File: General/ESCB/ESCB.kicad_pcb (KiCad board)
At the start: 2 copper layers, 37.4 x 21.6 mm, 3 parts, among them J1 Power_Signal, J2 Motor, U1 BESC

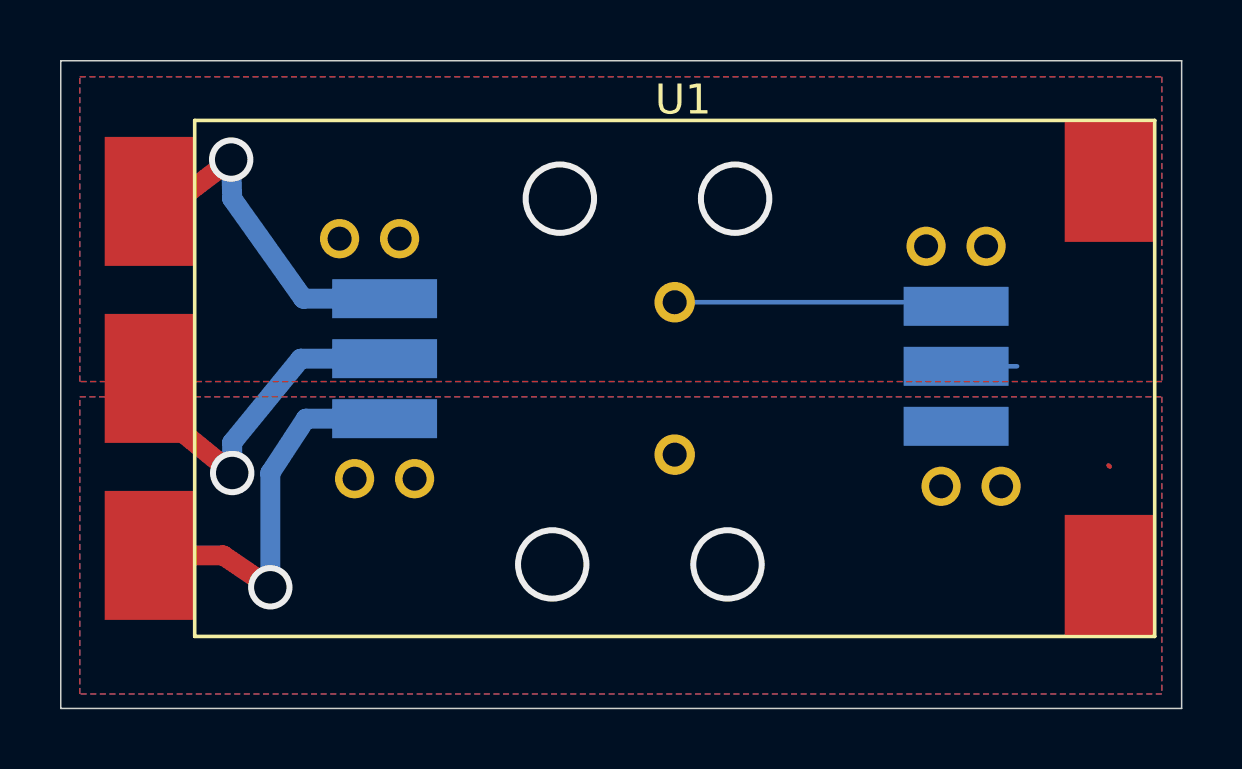
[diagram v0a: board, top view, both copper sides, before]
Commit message: via stitches, multiple vias for power, re-layout of copper pores
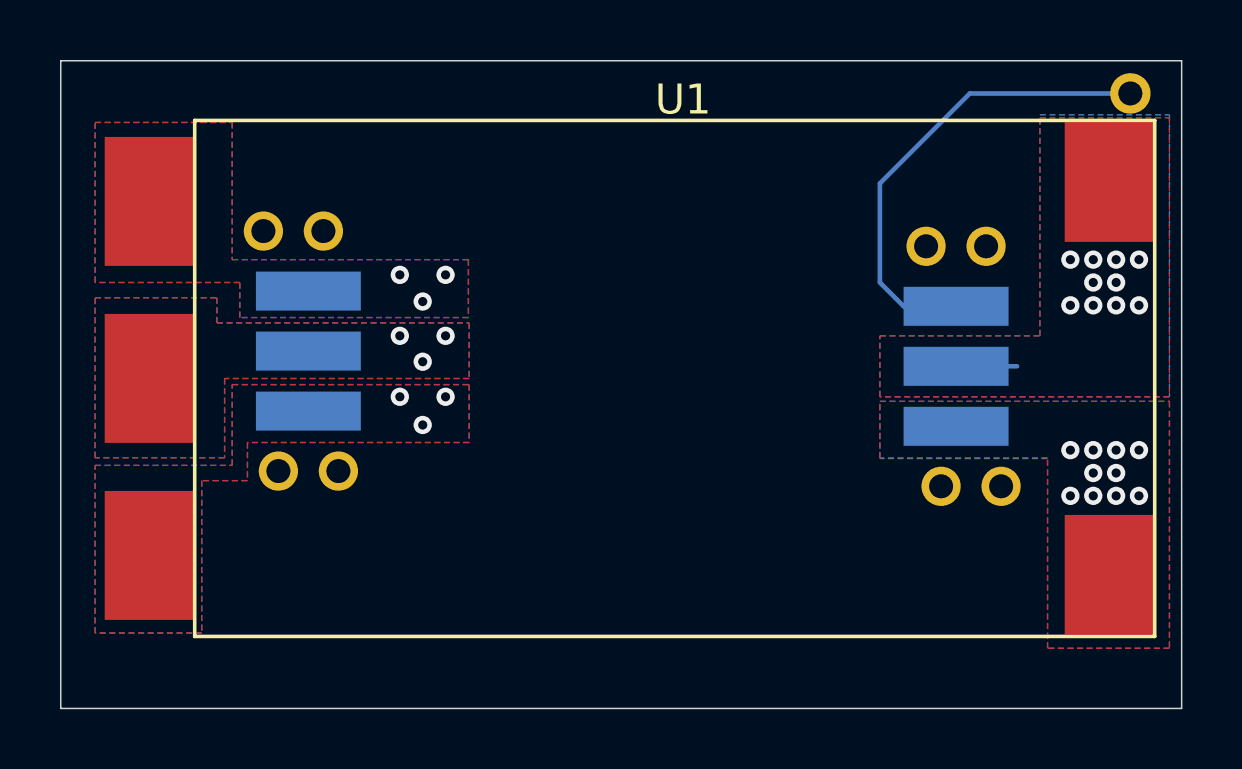
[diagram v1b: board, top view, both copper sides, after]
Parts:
- moved J2 2.55 mm to (129.5, 100.8)
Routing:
- net Net-(J2-Pad3): track 12.1 -> 0.00 mm, vias 1 -> 3
- net Net-(J2-Pad2): track 10.4 -> 0.91 mm, vias 1 -> 3
- net Net-(J2-Pad1): track 9.77 -> 0.88 mm, vias 1 -> 3
- net Net-(J1-Pad3): track 8.93 -> 16.0 mm
- net GND: track 0.06 -> 0.00 mm, vias 2 -> 10
- net VCC: vias 2 -> 10
- added copper zone on B.Cu, net Net-(J2-Pad1)
- added copper zone on F.Cu, net Net-(J2-Pad1)
- added copper zone on B.Cu, net Net-(J2-Pad2)
- added copper zone on F.Cu, net Net-(J2-Pad2)
- added copper zone on B.Cu, net Net-(J2-Pad3)
- added copper zone on F.Cu, net Net-(J2-Pad3)

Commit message: BESC Finishing Touches
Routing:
- net Net-(J1-Pad3): track 16.0 -> 7.61 mm
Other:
- board size 37.4 x 21.6 mm -> 35.8 x 17.5 mm
- board text added: "BESC"
